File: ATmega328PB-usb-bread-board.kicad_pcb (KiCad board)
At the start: 2 copper layers, 60 x 60 mm, 32 parts, among them J1 Conn_01x17, J2 Conn_01x17, J3 USB_B_Micro, J4 AVR-ISP-6, J5 Grove-I2C-connector, J6 Grove-I2C-connector, J7 Grove-I2C-connector, U1 ATmega328PB-MU, U2 CP2102N-A01-GQFN28, U3 LMV358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

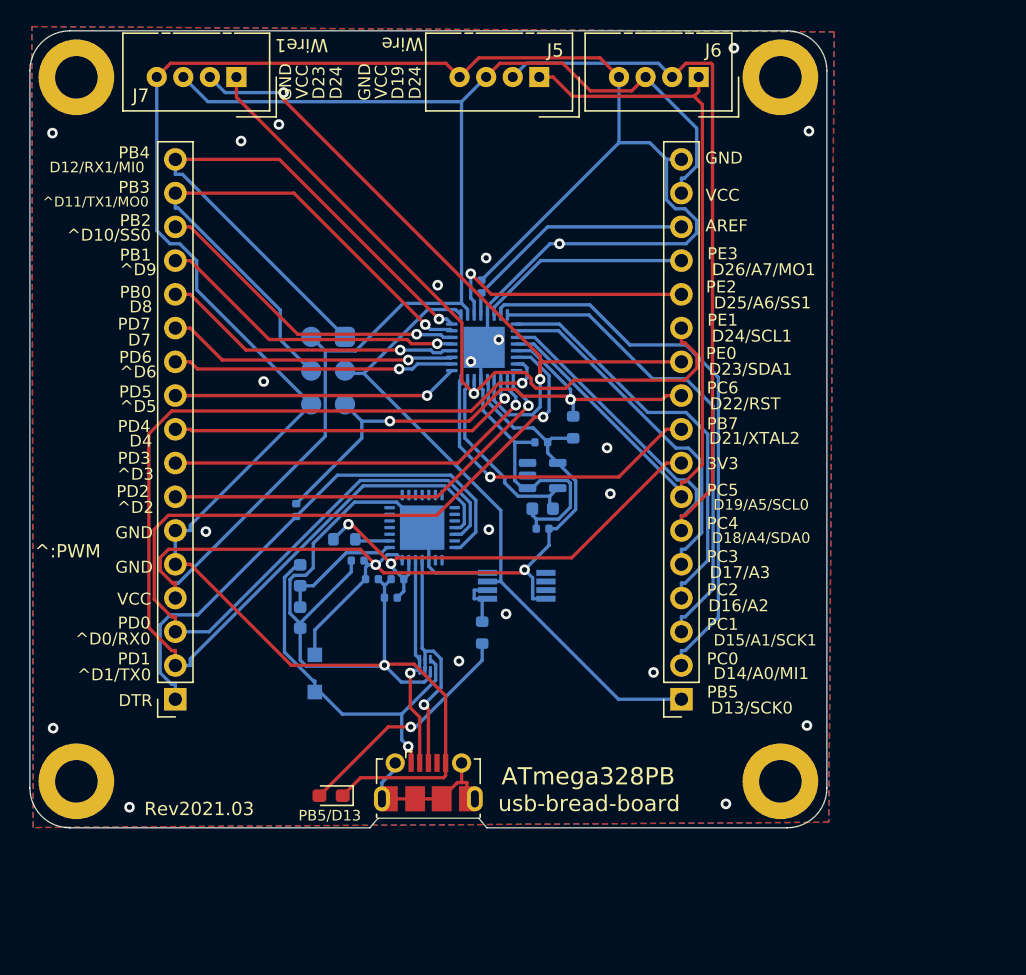
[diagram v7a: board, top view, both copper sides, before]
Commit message: Rename VCC label to 5V
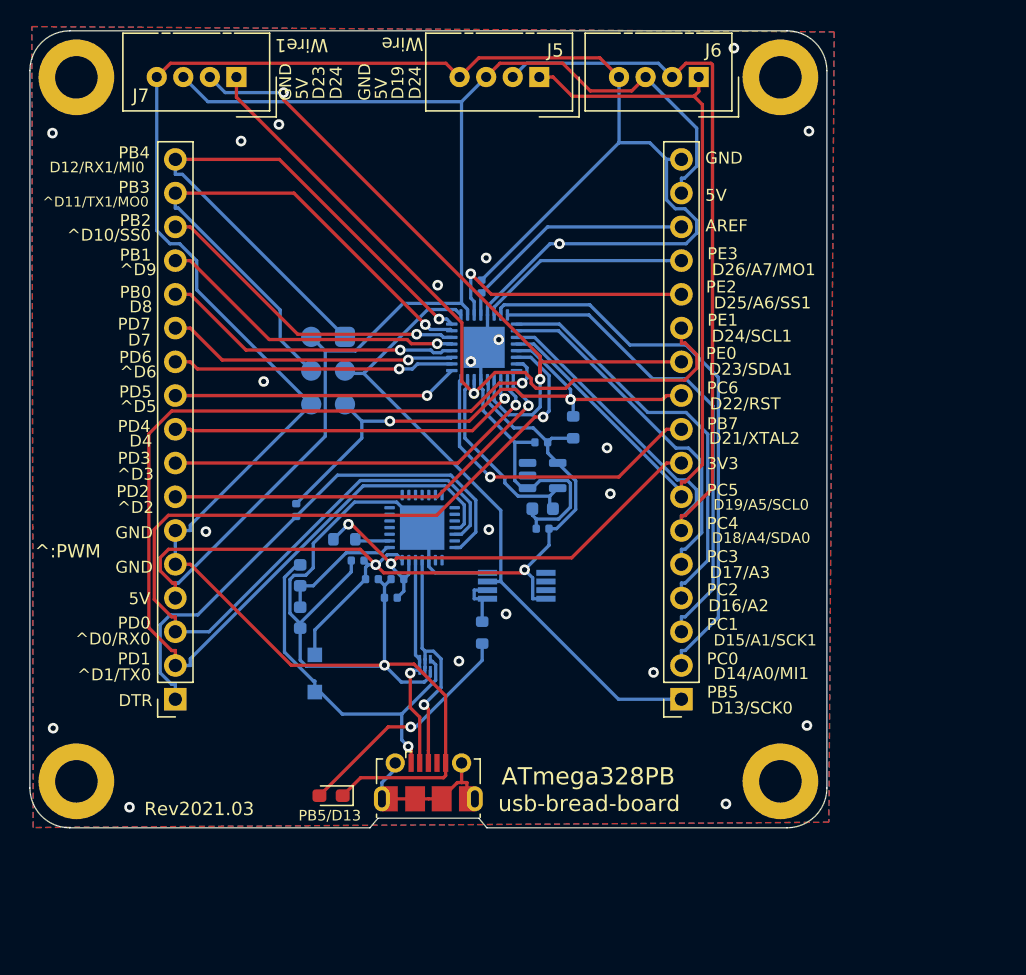
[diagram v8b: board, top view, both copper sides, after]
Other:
- board text added: "5V"
- board text removed: "VCC"
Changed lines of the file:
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@@
     )
   )
-  (gr_text VCC (at 126.45 53.85 90) (layer F.SilkS)
+  (gr_text 5V (at 126.45 54.35 90) (layer F.SilkS)
     (effects (font (size 0.9 0.9) (thickness 0.15)))
   )
@@
     (effects (font (size 0.9 0.9) (thickness 0.15)))
   )
-  (gr_text VCC (at 120.5 53.85 90) (layer F.SilkS)
+  (gr_text 5V (at 120.5 54.35 90) (layer F.SilkS)
     (effects (font (size 0.9 0.9) (thickness 0.15)))
   )
@@
     (effects (font (size 0.9 0.9) (thickness 0.15)))
   )
-  (gr_text VCC (at 152.15 62.38) (layer F.SilkS)
+  (gr_text 5V (at 151.65 62.38) (layer F.SilkS)
     (effects (font (size 0.9 0.9) (thickness 0.15)))
   )
@@
     (effects (font (size 0.9 0.9) (thickness 0.15)))
   )
-  (gr_text VCC (at 107.85 92.78) (layer F.SilkS)
-    (effects (font (size 0.9 0.9) (thickness 0.15)))
-  )
+  (gr_text 5V (at 108.25 92.75) (layer F.SilkS)
+    (effects (font (size 0.9 0.9) (thickness 0.15)))
+  )
